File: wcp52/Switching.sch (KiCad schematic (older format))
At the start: 11 parts, among them Q7 MMBT3906, Q8 2N7002, Q9 2N7002, U10 MASWSS0162, U9 MASWSS0162

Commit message: Reannotate parts. May need to tweak silkscreen
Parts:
- C57: renamed from C71; OldReference (none) -> C71
- C58: renamed from C72; OldReference (none) -> C72
- Q5: renamed from Q7; OldReference (none) -> Q7
- Q6: renamed from Q8; OldReference (none) -> Q8
- Q7: renamed from Q9; OldReference (none) -> Q9
- R65: renamed from R64; OldReference (none) -> R64
- R66: renamed from R6; OldReference (none) -> R6
- R67: renamed from R66; OldReference (none) -> R66
- R68: renamed from R67; OldReference (none) -> R67
- U8: renamed from U9; OldReference (none) -> U9
- U9: renamed from U10; OldReference (none) -> U10
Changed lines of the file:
@@
 $EndDescr
 $Comp
-L MASWSS0162 U9
+L MASWSS0162 U8
 U 1 1 54F34173
 P 6600 2500
-F 0 "U9" H 6250 2150 50  0000 C CNN
+F 0 "U8" H 6250 2150 50  0000 C CNN
 F 1 "MASWSS0162" H 6750 2150 50  0000 C CNN
 F 2 "IPC7351-Nominal:SOIC127P600X175-8" H 6600 2500 50  0001 C CNN
@@
 F 5 "MACom" H 6600 2500 60  0001 C CNN "Manuf"
 F 6 "MASWSS0162TR-3000" H 6700 3100 60  0001 C CNN "PN"
+F 7 "U9" H 6600 2500 50  0001 C CNN "OldReference"
 	1    6600 2500
 	1    0    0    -1
 $EndComp
 $Comp
-L MASWSS0162 U10
+L MASWSS0162 U9
 U 1 1 54F3428A
 P 6600 3300
-F 0 "U10" H 6250 2950 50  0000 C CNN
+F 0 "U9" H 6250 2950 50  0000 C CNN
 F 1 "MASWSS0162" H 6750 2950 50  0000 C CNN
 F 2 "IPC7351-Nominal:SOIC127P600X175-8" H 6600 3300 50  0001 C CNN
@@
 F 5 "MACom" H 6600 3300 60  0001 C CNN "Manuf"
 F 6 "MASWSS0162TR-3000" H 6700 3900 60  0001 C CNN "PN"
+F 7 "U10" H 6600 3300 50  0001 C CNN "OldReference"
 	1    6600 3300
 	1    0    0    -1
@@
 F 2 "" H 6700 4000 60  0000 C CNN
 F 3 "" H 6700 4000 60  0000 C CNN
+F 4 "#PWR0178" H 6700 4000 50  0001 C CNN "OldReference"
 	1    6700 4000
 	-1   0    0    1
@@
 F 2 "" H 7100 4000 60  0000 C CNN
 F 3 "" H 7100 4000 60  0000 C CNN
+F 4 "#PWR0179" H 7100 4000 50  0001 C CNN "OldReference"
 	1    7100 4000
 	-1   0    0    1
@@
 F 2 "" H 5400 4850 60  0000 C CNN
 F 3 "" H 5400 4850 60  0000 C CNN
+F 4 "#PWR0180" H 5400 4850 50  0001 C CNN "OldReference"
 	1    5400 4850
 	1    0    0    -1
@@
 F 2 "" H 5600 4850 60  0000 C CNN
 F 3 "" H 5600 4850 60  0000 C CNN
+F 4 "#PWR0181" H 5600 4850 50  0001 C CNN "OldReference"
 	1    5600 4850
 	1    0    0    -1
@@
 IN2
 $Comp
-L 2N7002 Q8
+L 2N7002 Q6
 U 1 1 54F3585D
 P 6650 6100
-F 0 "Q8" H 6800 6200 50  0000 C CNN
+F 0 "Q6" H 6800 6200 50  0000 C CNN
 F 1 "2N7002" H 6900 6050 50  0001 C CNN
 F 2 "smd-semi:SOT-23" H 6650 6100 50  0001 C CNN
@@
 F 4 "Value" H 6650 6100 60  0001 C CNN "Manuf"
 F 5 "#DIST DIGIKEY 568-5818-1-ND" H 7400 6650 60  0001 C CNN "BOM"
+F 6 "Q8" H 6650 6100 50  0001 C CNN "OldReference"
 	1    6650 6100
 	1    0    0    -1
 $EndComp
 $Comp
-L 2N7002 Q9
+L 2N7002 Q7
 U 1 1 54F359AE
 P 7050 6100
-F 0 "Q9" H 7300 6150 50  0000 C CNN
+F 0 "Q7" H 7300 6150 50  0000 C CNN
 F 1 "2N7002" H 7300 6050 50  0000 C CNN
 F 2 "smd-semi:SOT-23" H 7050 6100 50  0001 C CNN
@@
 F 4 "Value" H 7050 6100 60  0001 C CNN "Manuf"
 F 5 "#DIST DIGIKEY 568-5818-1-ND" H 7800 6650 60  0001 C CNN "BOM"
+F 6 "Q9" H 7050 6100 50  0001 C CNN "OldReference"
 	1    7050 6100
 	1    0    0    -1
@@
 F 2 "" H 6700 6250 60  0000 C CNN
 F 3 "" H 6700 6250 60  0000 C CNN
+F 4 "#PWR0182" H 6700 6250 50  0001 C CNN "OldReference"
 	1    6700 6250
 	1    0    0    -1
@@
 F 2 "" H 7100 6250 60  0000 C CNN
 F 3 "" H 7100 6250 60  0000 C CNN
+F 4 "#PWR0183" H 7100 6250 50  0001 C CNN "OldReference"
 	1    7100 6250
 	1    0    0    -1
@@
 F 2 "" H 6050 6450 60  0000 C CNN
 F 3 "" H 6050 6450 60  0000 C CNN
+F 4 "#PWR0184" H 6050 6450 50  0001 C CNN "OldReference"
 	1    6050 6450
 	1    0    0    -1
@@
 	6050 6450 6050 6400
 $Comp
-L MMBT3906 Q7
+L MMBT3906 Q5
 U 1 1 54F35F38
 P 6000 5900
-F 0 "Q7" H 6300 5950 50  0000 C CNN
+F 0 "Q5" H 6300 5950 50  0000 C CNN
 F 1 "MMBT3906" H 6300 5850 50  0000 C CNN
 F 2 "smd-semi:SOT-23" H 6000 5900 50  0001 C CNN
@@
 F 4 "Value" H 6000 5900 60  0001 C CNN "Manuf"
 F 5 "#DIST DIGIKEY MMBT3906LT1GOSCT-ND" H 6800 6450 60  0001 C CNN "BOM"
+F 6 "Q7" H 6000 5900 50  0001 C CNN "OldReference"
 	1    6000 5900
 	1    0    0    -1
@@
 F 2 "" H 5800 5900 60  0000 C CNN
 F 3 "" H 5800 5900 60  0000 C CNN
+F 4 "#PWR0185" H 5800 5900 50  0001 C CNN "OldReference"
 	1    5800 5900
 	0    1    1    0
@@
 F 2 "" H 7300 3600 60  0000 C CNN
 F 3 "" H 7300 3600 60  0000 C CNN
+F 4 "#PWR0186" H 7300 3600 50  0001 C CNN "OldReference"
 	1    7300 3600
 	1    0    0    -1
 $EndComp
 $Comp
-L RESPACK-4X0603-CONV R6
+L RESPACK-4X0603-CONV R66
 U 1 1 54FD633A
 P 6050 6300
-AR Path="/54F1FB16/54F2F9AC/54FD633A" Ref="R6"  Part="1"
-AR Path="/54F1FAFD/54FD633A" Ref="R6"  Part="4"
-F 0 "R6" H 5900 6250 50  0000 C CNN
+F 0 "R66" H 5900 6250 50  0000 C CNN
 F 1 "10k" H 5900 6350 50  0000 C CNN
 F 2 "IPC7351-Nominal:RESCAXE80P160X320X70-8" H 6050 6300 50  0001 C CNN
@@
 F 5 "Yageo" H 6050 6300 60  0001 C CNN "Manuf"
 F 6 "DIST DIGIKEY YC164J-10KCT-ND" H 6050 6300 60  0001 C CNN "BOM"
+F 7 "R6" H 6050 6300 50  0001 C CNN "OldReference"
 	1    6050 6300
 	-1   0    0    1
 $EndComp
 $Comp
-L RESPACK-4X0603-CONV R6
+L RESPACK-4X0603-CONV R66
 U 3 1 54FD63A4
 P 6700 4200
-F 0 "R6" H 6550 4150 50  0000 C CNN
+F 0 "R66" H 6550 4150 50  0000 C CNN
 F 1 "10k" H 6550 4250 50  0000 C CNN
 F 2 "IPC7351-Nominal:RESCAXE80P160X320X70-8" H 6700 4200 50  0001 C CNN
@@
 F 5 "Yageo" H 6700 4200 60  0001 C CNN "Manuf"
 F 6 "DIST DIGIKEY YC164J-10KCT-ND" H 6700 4200 60  0001 C CNN "BOM"
+F 7 "R6" H 6700 4200 50  0001 C CNN "OldReference"
 	3    6700 4200
 	-1   0    0    1
 $EndComp
 $Comp
-L RESPACK-4X0603-CONV R6
+L RESPACK-4X0603-CONV R66
 U 2 1 54FD63F6
 P 7100 4200
-F 0 "R6" H 6950 4150 50  0000 C CNN
+F 0 "R66" H 6950 4150 50  0000 C CNN
 F 1 "10k" H 6950 4250 50  0000 C CNN
 F 2 "IPC7351-Nominal:RESCAXE80P160X320X70-8" H 7100 4200 50  0001 C CNN
@@
 F 5 "Yageo" H 7100 4200 60  0001 C CNN "Manuf"
 F 6 "DIST DIGIKEY YC164J-10KCT-ND" H 7100 4200 60  0001 C CNN "BOM"
+F 7 "R6" H 7100 4200 50  0001 C CNN "OldReference"
 	2    7100 4200
 	-1   0    0    1
 $EndComp
 $Comp
-L R-0603 R64
+L R-0603 R65
 U 1 1 5504344E
 P 6050 5600
-F 0 "R64" H 6200 5650 50  0000 C CNN
+F 0 "R65" H 6200 5650 50  0000 C CNN
 F 1 "1k6" H 6200 5550 50  0000 C CNN
 F 2 "IPC7351-Nominal:RESC1608X50" H 6050 5600 50  0001 C CNN
@@
 F 4 "Value" H 6050 5600 60  0001 C CNN "Manuf"
 F 5 "RES SMD 1.6k 1% [0603]" H 6800 6150 60  0001 C CNN "BOM"
+F 6 "R64" H 6050 5600 50  0001 C CNN "OldReference"
 	1    6050 5600
 	1    0    0    -1
 $EndComp
 $Comp
-L R-0603 R67
+L R-0603 R68
 U 1 1 55044AA5
 P 6350 4400
-F 0 "R67" V 6150 4400 50  0000 C CNN
+F 0 "R68" V 6150 4400 50  0000 C CNN
 F 1 "200" V 6250 4400 50  0000 C CNN
 F 2 "IPC7351-Nominal:RESC1608X50" H 6350 4400 50  0001 C CNN
@@
 F 4 "Value" H 6350 4400 60  0001 C CNN "Manuf"
 F 5 "RES SMD 200 1% [0603]" H 7100 4950 60  0001 C CNN "BOM"
+F 6 "R67" H 6350 4400 50  0001 C CNN "OldReference"
 	1    6350 4400
 	0    1    1    0
 $EndComp
 $Comp
-L R-0603 R66
+L R-0603 R67
 U 1 1 55044C5F
 P 6100 4500
-F 0 "R66" V 5850 4500 50  0000 C CNN
+F 0 "R67" V 5850 4500 50  0000 C CNN
 F 1 "200" V 5950 4500 50  0000 C CNN
 F 2 "IPC7351-Nominal:RESC1608X50" H 6100 4500 50  0001 C CNN
@@
 F 4 "Value" H 6100 4500 60  0001 C CNN "Manuf"
 F 5 "RES SMD 200 1% [0603]" H 6850 5050 60  0001 C CNN "BOM"
+F 6 "R66" H 6100 4500 50  0001 C CNN "OldReference"
 	1    6100 4500
 	0    1    1    0
 $EndComp
 $Comp
-L C-0603 C71
+L C-0603 C57
 U 1 1 55046FF6
 P 5400 4700
-F 0 "C71" H 5600 4750 50  0000 C CNN
+F 0 "C57" H 5600 4750 50  0000 C CNN
 F 1 "1n" H 5600 4650 50  0000 C CNN
 F 2 "IPC7351-Nominal:CAPC1608X55" H 5400 4700 50  0001 C CNN
@@
 F 4 "Value" H 5400 4700 60  0001 C CNN "Manuf"
 F 5 "CAP MLCC 1n C0G 50V 10% [0603]" H 6200 5250 60  0001 C CNN "BOM"
+F 6 "C71" H 5400 4700 50  0001 C CNN "OldReference"
 	1    5400 4700
 	-1   0    0    -1
 $EndComp
 $Comp
-L C-0603 C72
+L C-0603 C58
 U 1 1 55047017
 P 5600 4700
-F 0 "C72" H 5800 4750 50  0000 C CNN
+F 0 "C58" H 5800 4750 50  0000 C CNN
 F 1 "1n" H 5800 4650 50  0000 C CNN
 F 2 "IPC7351-Nominal:CAPC1608X55" H 5600 4700 50  0001 C CNN
@@
 F 4 "Value" H 5600 4700 60  0001 C CNN "Manuf"
 F 5 "CAP MLCC 1n C0G 50V 10% [0603]" H 6400 5250 60  0001 C CNN "BOM"
+F 6 "C72" H 5600 4700 50  0001 C CNN "OldReference"
 	1    5600 4700
 	1    0    0    -1

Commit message: Schematic touchups
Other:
- note added: "Inside shield"
- note added: "Outside shield"
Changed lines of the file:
@@
 Sheet 8 13
 Title "Input Switching"
-Date "2015-03-10"
+Date "2015-03-13"
 Rev ""
 Comp "WCP52"
@@
 Text HLabel 8400 2700 2    60   Output ~ 0
 OUT
-Text Notes 7950 2850 0    60   ~ 0
+Text Notes 7950 2850 0    50   ~ 0
 Layout: These stubs must be /very/ short!
 $Comp
@@
 	1    0    0    -1
 $EndComp
+Text Notes 3150 5100 0    50   ~ 0
+Inside shield
+Text Notes 3150 5200 0    50   ~ 0
+Outside shield
 $EndSCHEMATC

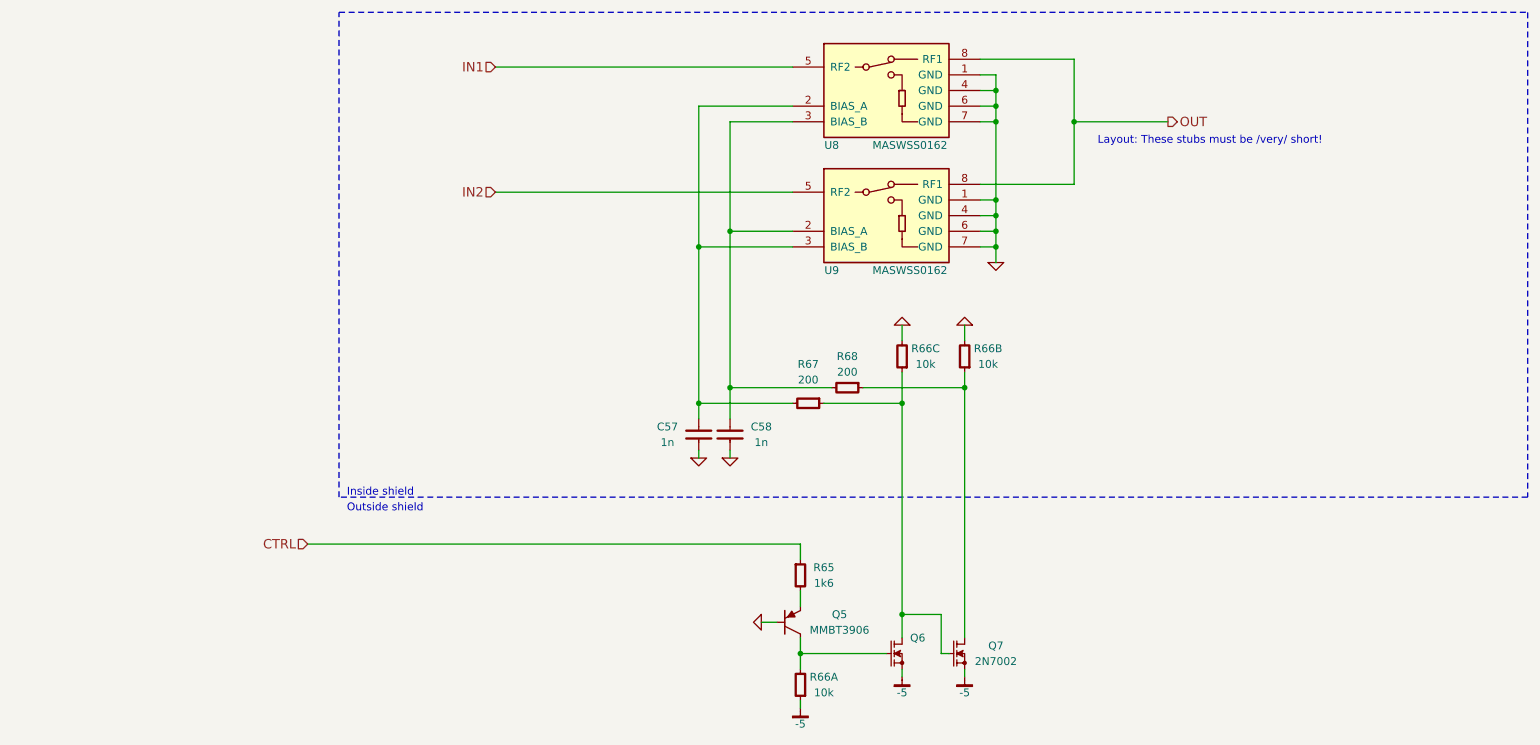
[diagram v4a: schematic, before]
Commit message: Change schematic pages to letter size
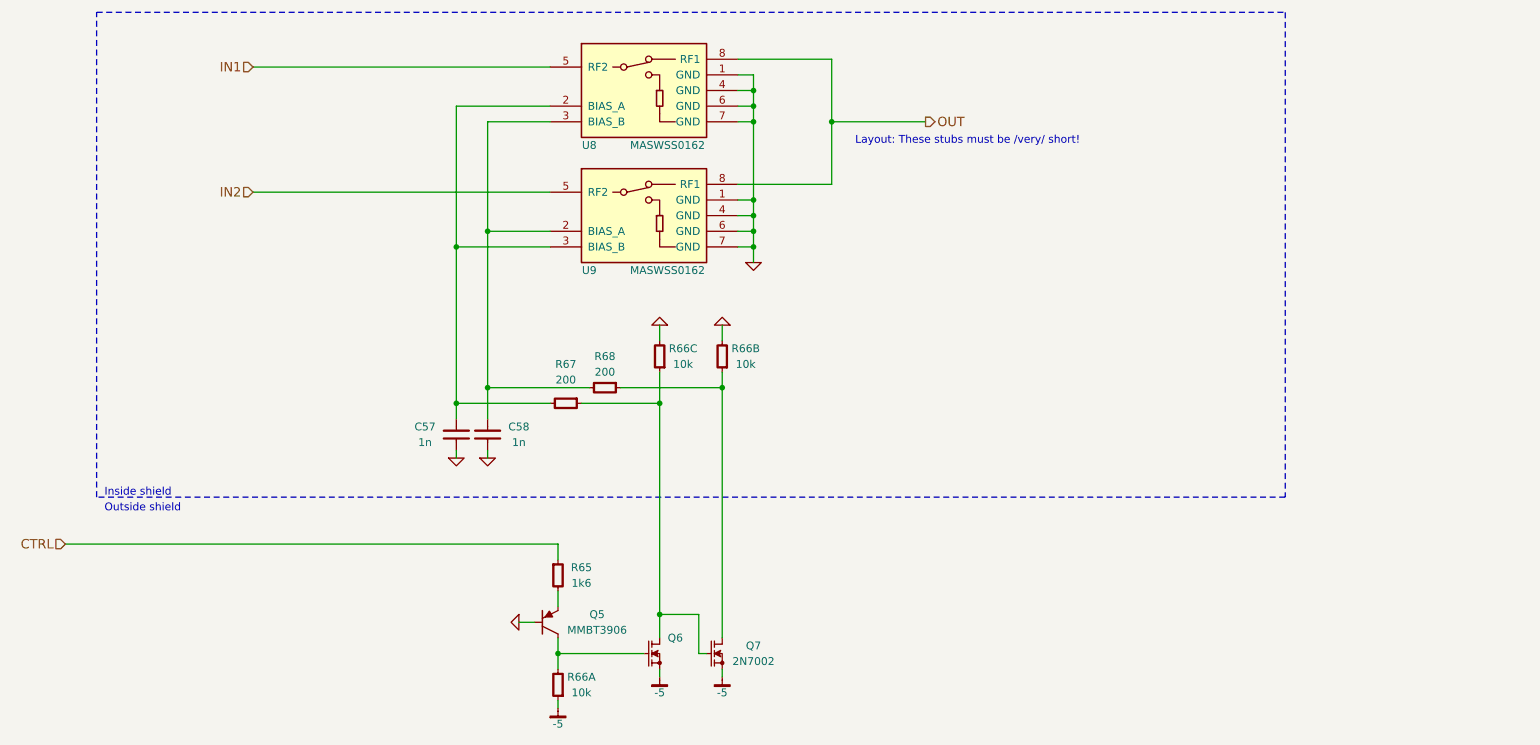
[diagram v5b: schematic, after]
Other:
- moved on the sheet: C57, C58, Q5, Q6, Q7, R65, R66A, R66B, R66C, R67, R68, U8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

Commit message: BOM fixes
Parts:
- U8, U9: BOM DIST DIGIKEY 1465-1381-1-ND -> IC MACOM MASWSS0162
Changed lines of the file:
@@
 EESchema Schematic File Version 2
-LIBS:Altera
-LIBS:AnalogDevices
-LIBS:Atmel
-LIBS:conn-2mm
-LIBS:conn-100mil
-LIBS:conn-cui
-LIBS:conn-fci
-LIBS:conn-linx
-LIBS:conn-molex
-LIBS:conn-tagconnect
-LIBS:conn-test
-LIBS:DiodesInc
-LIBS:display
-LIBS:_electromech
-LIBS:Fairchild
-LIBS:FTDI
-LIBS:Intersil
-LIBS:Lattice
-LIBS:_linear
-LIBS:LinearTech
-LIBS:Littelfuse
-LIBS:logic-4000
-LIBS:logic-7400
-LIBS:MACOM
-LIBS:maxim
-LIBS:mechanical
-LIBS:Microchip
-LIBS:Micron
-LIBS:NXP
-LIBS:onsemi
-LIBS:passive
-LIBS:pasv-BiTech
-LIBS:pasv-Bourns
-LIBS:pasv-cap
-LIBS:pasv-ind
-LIBS:pasv-res
-LIBS:pcb
-LIBS:power
-LIBS:_semi
-LIBS:semi-diode-1N
-LIBS:semi-diode-BA
-LIBS:semi-diode-MCC
-LIBS:semi-diode-MMB
-LIBS:semi-diode-NXP
-LIBS:semi-diode-OnSemi
-LIBS:semi-diode-Vishay
-LIBS:semi-opto-misc
-LIBS:semi-thyristor-2N
-LIBS:semi-trans-2N
-LIBS:semi-trans-AO
-LIBS:semi-trans-BC
-LIBS:semi-trans-DiodesInc
-LIBS:semi-trans-Fairchild
-LIBS:semi-trans-Infineon
-LIBS:semi-trans-IntRect
-LIBS:semi-trans-IXYS
-LIBS:semi-trans-misc
-LIBS:semi-trans-MMB
-LIBS:semi-trans-MPS
-LIBS:semi-trans-NXP
-LIBS:semi-trans-PZT
-LIBS:semi-trans-TI
-LIBS:semi-trans-TIP
-LIBS:semi-trans-Toshiba
-LIBS:silabs
-LIBS:skyworks
-LIBS:ST
-LIBS:st_ic
-LIBS:st_semi
-LIBS:supertex
-LIBS:symbol
-LIBS:TexasInstruments
-LIBS:vishay_semi
-LIBS:Xilinx
-LIBS:pasv-xtal
-LIBS:conn-te
 LIBS:wcp52-cache
 EELAYER 25 0
@@
 F 2 "IPC7351-Nominal:SOIC127P600X175-8" H 5050 2500 50  0001 C CNN
 F 3 "" H 5000 2650 60  0000 C CNN
-F 4 "DIST DIGIKEY 1465-1381-1-ND" H 5550 3500 60  0001 C CNN "BOM"
+F 4 "MASWSS0162TR-3000" H 5150 3100 60  0001 C CNN "PN"
 F 5 "MACom" H 5050 2500 60  0001 C CNN "Manuf"
-F 6 "MASWSS0162TR-3000" H 5150 3100 60  0001 C CNN "PN"
+F 6 "IC MACOM MASWSS0162" H 5550 3500 60  0001 C CNN "BOM"
 F 7 "U9" H 5050 2500 50  0001 C CNN "OldReference"
 	1    5050 2500
@@
 F 2 "IPC7351-Nominal:SOIC127P600X175-8" H 5050 3300 50  0001 C CNN
 F 3 "" H 5000 3450 60  0000 C CNN
-F 4 "DIST DIGIKEY 1465-1381-1-ND" H 5550 4300 60  0001 C CNN "BOM"
+F 4 "MASWSS0162TR-3000" H 5150 3900 60  0001 C CNN "PN"
 F 5 "MACom" H 5050 3300 60  0001 C CNN "Manuf"
-F 6 "MASWSS0162TR-3000" H 5150 3900 60  0001 C CNN "PN"
+F 6 "IC MACOM MASWSS0162" H 5550 4300 60  0001 C CNN "BOM"
 F 7 "U10" H 5050 3300 50  0001 C CNN "OldReference"
 	1    5050 3300

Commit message: BOM line fixes
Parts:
- C57, C58, Q5, Q6, Q7, R65, R67, R68: Manuf Value -> (none)
- R66: Description (none) -> RESPACK SMD 10k 5% [4x0603]
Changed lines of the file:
@@
 EESchema Schematic File Version 2
+LIBS:Altera
+LIBS:AnalogDevices
+LIBS:Atmel
+LIBS:conn-2mm
+LIBS:conn-100mil
+LIBS:conn-cui
+LIBS:conn-fci
+LIBS:conn-linx
+LIBS:conn-molex
+LIBS:conn-tagconnect
+LIBS:conn-test
+LIBS:DiodesInc
+LIBS:display
+LIBS:_electromech
+LIBS:Fairchild
+LIBS:FTDI
+LIBS:Intersil
+LIBS:Lattice
+LIBS:_linear
+LIBS:LinearTech
+LIBS:Littelfuse
+LIBS:logic-4000
+LIBS:logic-7400
+LIBS:MACOM
+LIBS:maxim
+LIBS:mechanical
+LIBS:Microchip
+LIBS:Micron
+LIBS:NXP
+LIBS:onsemi
+LIBS:passive
+LIBS:pasv-BiTech
+LIBS:pasv-Bourns
+LIBS:pasv-cap
+LIBS:pasv-ind
+LIBS:pasv-res
+LIBS:pcb
+LIBS:power
+LIBS:_semi
+LIBS:semi-diode-1N
+LIBS:semi-diode-BA
+LIBS:semi-diode-MCC
+LIBS:semi-diode-MMB
+LIBS:semi-diode-NXP
+LIBS:semi-diode-OnSemi
+LIBS:semi-diode-Vishay
+LIBS:semi-opto-misc
+LIBS:semi-thyristor-2N
+LIBS:semi-trans-2N
+LIBS:semi-trans-AO
+LIBS:semi-trans-BC
+LIBS:semi-trans-DiodesInc
+LIBS:semi-trans-Fairchild
+LIBS:semi-trans-Infineon
+LIBS:semi-trans-IntRect
+LIBS:semi-trans-IXYS
+LIBS:semi-trans-misc
+LIBS:semi-trans-MMB
+LIBS:semi-trans-MPS
+LIBS:semi-trans-NXP
+LIBS:semi-trans-PZT
+LIBS:semi-trans-TI
+LIBS:semi-trans-TIP
+LIBS:semi-trans-Toshiba
+LIBS:silabs
+LIBS:skyworks
+LIBS:ST
+LIBS:st_ic
+LIBS:st_semi
+LIBS:supertex
+LIBS:symbol
+LIBS:TexasInstruments
+LIBS:vishay_semi
+LIBS:Xilinx
+LIBS:pasv-xtal
+LIBS:conn-te
 LIBS:wcp52-cache
 EELAYER 25 0
@@
 F 2 "smd-semi:SOT-23" H 5100 6100 50  0001 C CNN
 F 3 "" H 5100 6100 60  0000 C CNN
-F 4 "Value" H 5100 6100 60  0001 C CNN "Manuf"
+F 4 "" H 5100 6100 60  0001 C CNN "Manuf"
 F 5 "#DIST DIGIKEY 568-5818-1-ND" H 5850 6650 60  0001 C CNN "BOM"
 F 6 "Q8" H 5100 6100 50  0001 C CNN "OldReference"
@@
 F 2 "smd-semi:SOT-23" H 5500 6100 50  0001 C CNN
 F 3 "" H 5500 6100 60  0000 C CNN
-F 4 "Value" H 5500 6100 60  0001 C CNN "Manuf"
+F 4 "" H 5500 6100 60  0001 C CNN "Manuf"
 F 5 "#DIST DIGIKEY 568-5818-1-ND" H 6250 6650 60  0001 C CNN "BOM"
 F 6 "Q9" H 5500 6100 50  0001 C CNN "OldReference"
@@
 F 2 "smd-semi:SOT-23" H 4450 5900 50  0001 C CNN
 F 3 "" H 4450 5900 60  0000 C CNN
-F 4 "Value" H 4450 5900 60  0001 C CNN "Manuf"
+F 4 "" H 4450 5900 60  0001 C CNN "Manuf"
 F 5 "#DIST DIGIKEY MMBT3906LT1GOSCT-ND" H 5250 6450 60  0001 C CNN "BOM"
 F 6 "Q7" H 4450 5900 50  0001 C CNN "OldReference"
@@
 F 5 "Yageo" H 4500 6300 60  0001 C CNN "Manuf"
 F 6 "DIST DIGIKEY YC164J-10KCT-ND" H 4500 6300 60  0001 C CNN "BOM"
-F 7 "R6" H 4500 6300 50  0001 C CNN "OldReference"
+F 7 "RESPACK SMD 10k 5% [4x0603]" H 4500 6300 60  0001 C CNN "Description"
+F 8 "R6" H 4500 6300 50  0001 C CNN "OldReference"
 	1    4500 6300
 	-1   0    0    1
@@
 F 5 "Yageo" H 5150 4200 60  0001 C CNN "Manuf"
 F 6 "DIST DIGIKEY YC164J-10KCT-ND" H 5150 4200 60  0001 C CNN "BOM"
-F 7 "R6" H 5150 4200 50  0001 C CNN "OldReference"
+F 7 "RESPACK SMD 10k 5% [4x0603]" H 5150 4200 60  0001 C CNN "Description"
+F 8 "R6" H 5150 4200 50  0001 C CNN "OldReference"
 	3    5150 4200
 	-1   0    0    1
@@
 F 5 "Yageo" H 5550 4200 60  0001 C CNN "Manuf"
 F 6 "DIST DIGIKEY YC164J-10KCT-ND" H 5550 4200 60  0001 C CNN "BOM"
-F 7 "R6" H 5550 4200 50  0001 C CNN "OldReference"
+F 7 "RESPACK SMD 10k 5% [4x0603]" H 5550 4200 60  0001 C CNN "Description"
+F 8 "R6" H 5550 4200 50  0001 C CNN "OldReference"
 	2    5550 4200
 	-1   0    0    1
@@
 F 2 "IPC7351-Nominal:RESC1608X50" H 4500 5600 50  0001 C CNN
 F 3 "" H 4500 5650 60  0000 C CNN
-F 4 "Value" H 4500 5600 60  0001 C CNN "Manuf"
+F 4 "" H 4500 5600 60  0001 C CNN "Manuf"
 F 5 "RES SMD 1.6k 1% [0603]" H 5250 6150 60  0001 C CNN "BOM"
 F 6 "R64" H 4500 5600 50  0001 C CNN "OldReference"
@@
 F 2 "IPC7351-Nominal:RESC1608X50" H 4800 4400 50  0001 C CNN
 F 3 "" H 4800 4450 60  0000 C CNN
-F 4 "Value" H 4800 4400 60  0001 C CNN "Manuf"
+F 4 "" H 4800 4400 60  0001 C CNN "Manuf"
 F 5 "RES SMD 200 1% [0603]" H 5550 4950 60  0001 C CNN "BOM"
 F 6 "R67" H 4800 4400 50  0001 C CNN "OldReference"
@@
 F 2 "IPC7351-Nominal:RESC1608X50" H 4550 4500 50  0001 C CNN
 F 3 "" H 4550 4550 60  0000 C CNN
-F 4 "Value" H 4550 4500 60  0001 C CNN "Manuf"
+F 4 "" H 4550 4500 60  0001 C CNN "Manuf"
 F 5 "RES SMD 200 1% [0603]" H 5300 5050 60  0001 C CNN "BOM"
 F 6 "R66" H 4550 4500 50  0001 C CNN "OldReference"
@@
 F 2 "IPC7351-Nominal:CAPC1608X55" H 3850 4700 50  0001 C CNN
 F 3 "" H 3840 4675 60  0000 C CNN
-F 4 "Value" H 3850 4700 60  0001 C CNN "Manuf"
+F 4 "" H 3850 4700 60  0001 C CNN "Manuf"
 F 5 "CAP MLCC 1n C0G 50V 10% [0603]" H 4650 5250 60  0001 C CNN "BOM"
 F 6 "C71" H 3850 4700 50  0001 C CNN "OldReference"
@@
 F 2 "IPC7351-Nominal:CAPC1608X55" H 4050 4700 50  0001 C CNN
 F 3 "" H 4040 4675 60  0000 C CNN
-F 4 "Value" H 4050 4700 60  0001 C CNN "Manuf"
+F 4 "" H 4050 4700 60  0001 C CNN "Manuf"
 F 5 "CAP MLCC 1n C0G 50V 10% [0603]" H 4850 5250 60  0001 C CNN "BOM"
 F 6 "C72" H 4050 4700 50  0001 C CNN "OldReference"

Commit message: BOM corrections/combinations, etc
Add configuration for bomtool
Remove old schematic file no longer used
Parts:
- Q5: BOM #DIST DIGIKEY MMBT3906LT1GOSCT-ND -> SEMI GENERIC MMBT3906
- Q6, Q7: BOM #DIST DIGIKEY 568-5818-1-ND -> SEMI GENERIC 2N7002
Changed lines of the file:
@@
 F 2 "smd-semi:SOT-23" H 5100 6100 50  0001 C CNN
 F 3 "" H 5100 6100 60  0000 C CNN
-F 4 "" H 5100 6100 60  0001 C CNN "Manuf"
-F 5 "#DIST DIGIKEY 568-5818-1-ND" H 5850 6650 60  0001 C CNN "BOM"
-F 6 "Q8" H 5100 6100 50  0001 C CNN "OldReference"
+F 4 "SEMI GENERIC 2N7002" H 5850 6650 60  0001 C CNN "BOM"
+F 5 "Q8" H 5100 6100 50  0001 C CNN "OldReference"
 	1    5100 6100
 	1    0    0    -1
@@
 F 2 "smd-semi:SOT-23" H 5500 6100 50  0001 C CNN
 F 3 "" H 5500 6100 60  0000 C CNN
-F 4 "" H 5500 6100 60  0001 C CNN "Manuf"
-F 5 "#DIST DIGIKEY 568-5818-1-ND" H 6250 6650 60  0001 C CNN "BOM"
-F 6 "Q9" H 5500 6100 50  0001 C CNN "OldReference"
+F 4 "SEMI GENERIC 2N7002" H 6250 6650 60  0001 C CNN "BOM"
+F 5 "Q9" H 5500 6100 50  0001 C CNN "OldReference"
 	1    5500 6100
 	1    0    0    -1
@@
 F 2 "smd-semi:SOT-23" H 4450 5900 50  0001 C CNN
 F 3 "" H 4450 5900 60  0000 C CNN
-F 4 "" H 4450 5900 60  0001 C CNN "Manuf"
-F 5 "#DIST DIGIKEY MMBT3906LT1GOSCT-ND" H 5250 6450 60  0001 C CNN "BOM"
-F 6 "Q7" H 4450 5900 50  0001 C CNN "OldReference"
+F 4 "SEMI GENERIC MMBT3906" H 5250 6450 60  0001 C CNN "BOM"
+F 5 "Q7" H 4450 5900 50  0001 C CNN "OldReference"
 	1    4450 5900
 	1    0    0    -1
